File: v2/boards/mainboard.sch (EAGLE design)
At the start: 190 parts, among them IC1 LM2596S-ADJ, IC10 DRV8835, IC11 TSOP324, IC12 ESP-WROOM-32, IC13 PAM8403, IC15 MC1525, IC16 INA282, IC17 INA282, IC18 INA282, IC19 INA282, IC2 LM2596S-5.0, IC20 MCP3008, IC3 LD1117A, IC4 LM393, IC5 MCP101-300, IC6 TEENSY 3.6, IC7 PCA9634, IC8 PCA9554, IC9 PCA9634, J1 Bat_In, J10 SPI_0, J11 SPI_2, J12 SPI_2, J13 I2C_0, J14 I2C_1, J15 I2C_3, J16 BNO055, J17 Uart_2, J18 Uart_5, J19 Uart_6 (LP), J2 Erw_Pwr, J20 BPS, J21 Servo_2, J22 Servo_3, J23 Erw_Servo, J24 Erw_PWM, J25 ESP32_Uart, J26 SPEAKER_L, J27 SPEAKER_R, J28 AUDIO_TEENSY, J29 SWD, J3 I2C0_5V, J30 SWD_KL02, J31 Erw_ENA, J32 Erw_GPIO, J33 Erw_analog, J34 USB_Host, J35 ESP32_PROG, J4 I2C3_5V, J5 Servo_1, J6 H-Bridge Mode, J7 RC5_SEL, J8 SPI_0, J9 SPI_0, SW1 TL32PO, U1 IRL3103, U4 BS108, U5 BS108, U6 BS108, U7 BS108, U8 BS108, U9 BS108, X1 max. 18V

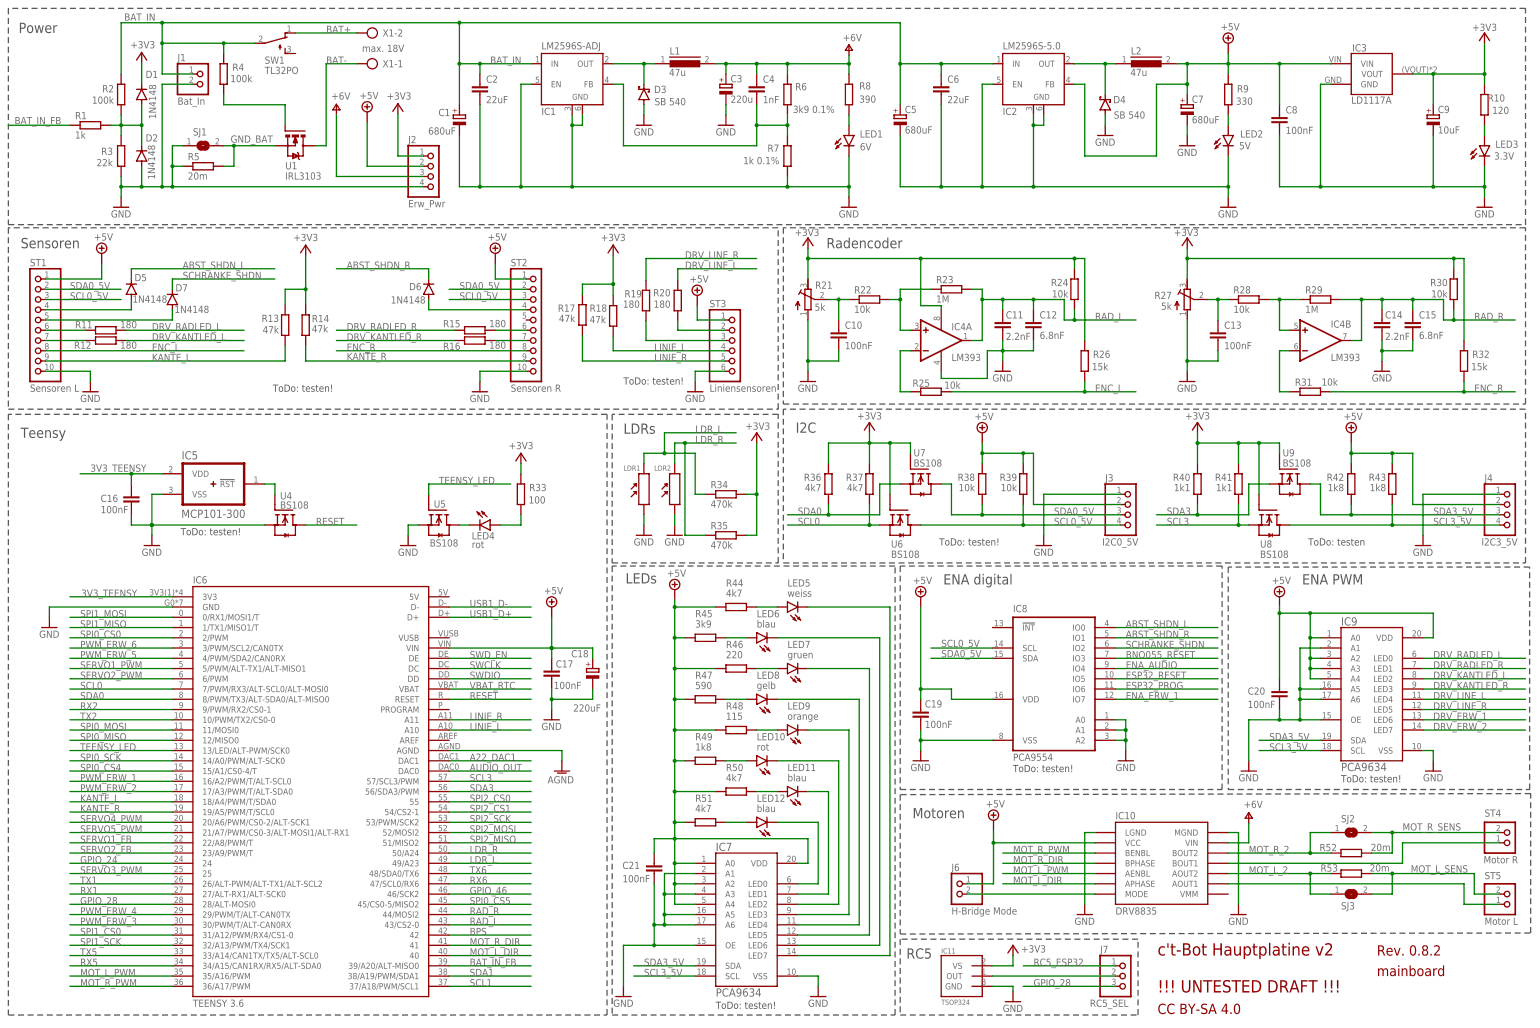
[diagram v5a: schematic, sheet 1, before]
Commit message: mainboard updated:
- some bugfixes after further testing
- discrete MCU board added
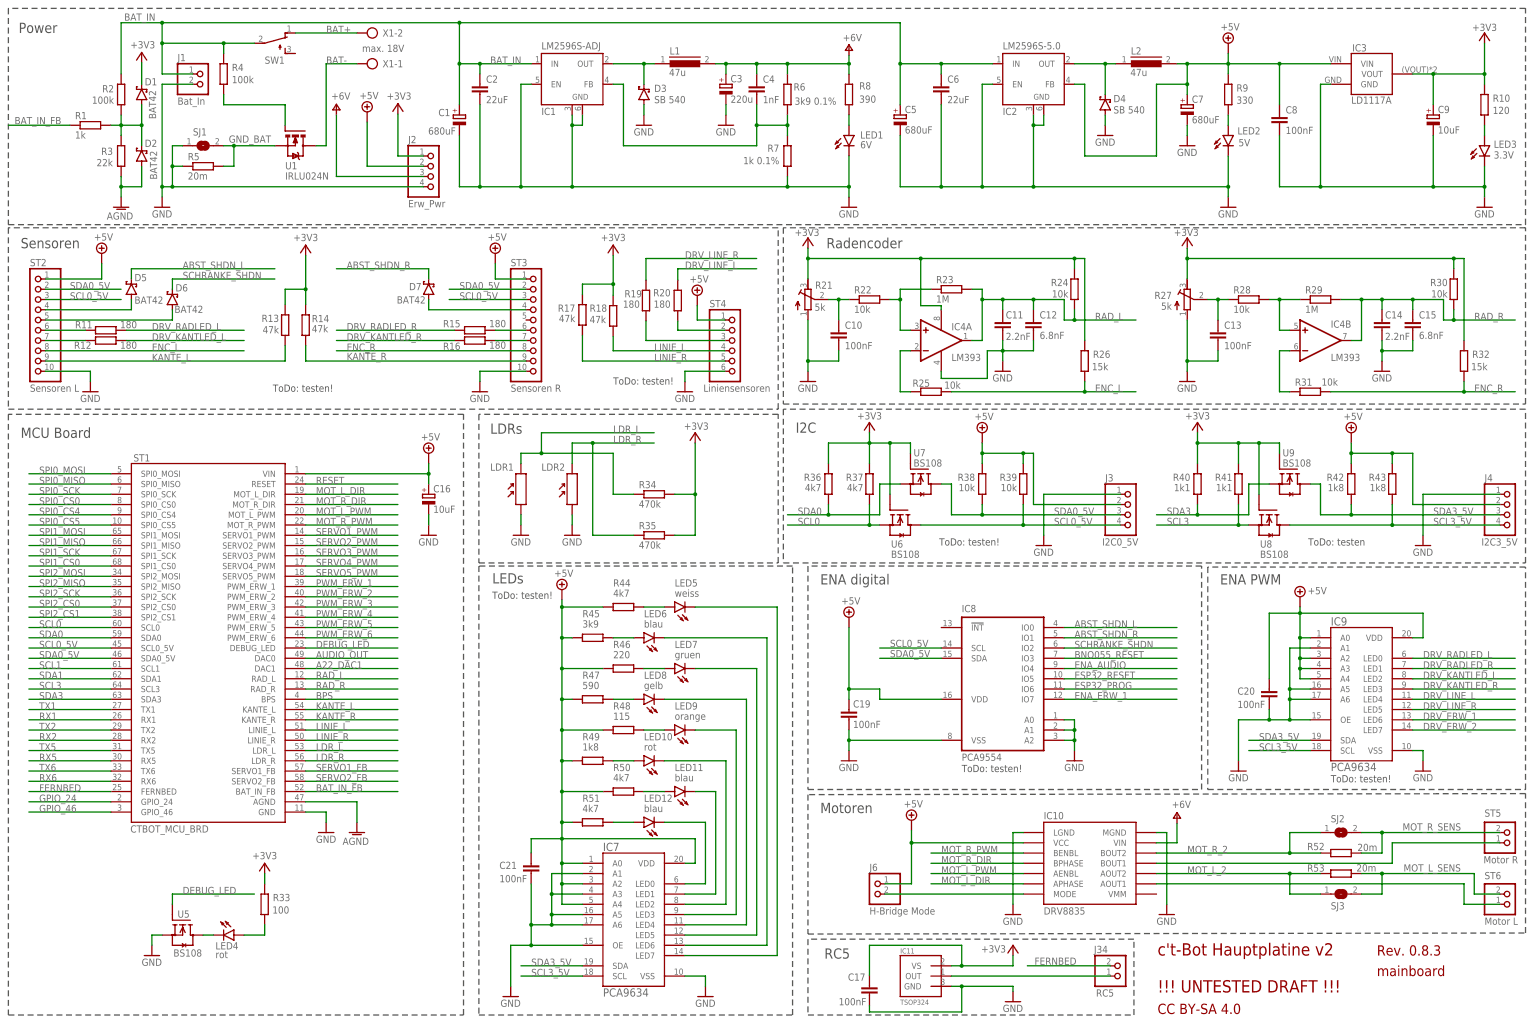
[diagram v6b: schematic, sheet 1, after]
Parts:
- removed BT1: CR2032, ct-bot:BATTERY-20MM_PTH
- removed IC5: MCP101-300, ct-bot:MCP101
- removed IC6: TEENSY 3.6, ct-bot:TEENSY3_6
- removed U4: BS108, ct-bot:BS108
- added J36: SPI1, ct-bot:PINHD-1X5
- added ST7: RPI_Interface, con-harting-ml:ML20
- C16: value 100nF -> 10uF; device rcl:C-EU025-025X050 -> rcl:CPOL-EUTT2D5L
- C18: value 220uF -> 100nF; device rcl:CPOL-EUE2-5 -> rcl:C-EU025-025X050
- D1, D2: value 1N4148 -> BAT42; device ct-bot:1N41480207/2V -> ct-bot:BAT42DO35-7
- D5, D6, D7, D8, D9: value 1N4148 -> BAT42; device ct-bot:1N41480207/2V -> ct-bot:BAT42"
- J29: device ct-bot:PINHD-1X6 -> ct-bot:PINHD-1X5
- J30: device ct-bot:PINHD90-1X2/90 -> ct-bot:PINHD-1X2
- J34: value USB_Host -> RC5; device ct-bot:PINHD-1X4 -> ct-bot:PINHD-1X2
- J7: value RC5_SEL -> ESP32_GPIO; SPICEPREFIX (none) -> J
- R1, R3, R55, R56, R57: device rcl:R-EU_0204/2V -> rcl:R-EU_0204/7
- R31, R32, R62: device rcl:R-EU_0204/7 -> rcl:R-EU_0204/2V
- ST1: value Sensoren L -> CTBOT_MCU_BRD; device ct-bot:PS25-10PS25-10 -> ct-bot:CTBOT_MCU_BRD
- ST2: value Sensoren R -> Sensoren L
- ST3: value Liniensensoren -> Sensoren R; device ct-bot:PS25-6 -> ct-bot:PS25-10PS25-10
- ST4: value Motor R -> Liniensensoren; device ct-bot:PINHD90-1X2/90 -> ct-bot:PS25-6
- ST5: value Motor L -> Motor R
- ST6: value RPI_Interface -> Motor L; device con-harting-ml:ML26 -> ct-bot:PINHD90-1X2/90
- U1: value IRL3103 -> IRLU024N; device ct-bot:IRF740 -> ct-bot:IRLU024NTO-251AA
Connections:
- removed net +5V: C17.1, C18.+, C19.1, C20.1, C21.1, C24.1, C25.1, C28.1, C29.+, C7.+, C8.1, IC10.VCC, IC13.PVDD, IC13.PVDD1, IC13.VDD, IC2.FB, IC3.VIN, IC6.VIN, IC7.A0, IC7.A2, IC7.A4, IC7.VDD, IC8.VDD, IC9.A0, IC9.A2, IC9.A3, IC9.A4, IC9.VDD, J10.1, J11.2, J12.2, J13.2, J14.2, J15.2, J16.1, J17.2, J18.2, J19.2, J2.2, J3.2, J34.1, J4.2, J6.1, J8.1, J9.1, L2.2, R38.2, R39.2, R42.2, R43.2, R44.1, R45.1, R46.1, R47.1, R48.1, R49.1, R50.1, R51.1, R9.2, ST1.1, ST2.1, ST3.1, ST6.23, ST6.25
- removed net 3V3_TEENSY: C16.1, IC5.VDD, IC6.3V3, J29.1
- removed net GPIO_28: IC6.28/ALT-MOSI0, J7.3
- removed net N$39: IC5.!RST, U4.G
- removed net RC5_ESP32: IC12.IO23, J7.1
- removed net SERVO3_FB: ST6.14
- removed net TEENSY_LED: IC6.13/LED/ALT-PWM/SCK0, U5.G
- removed net USB1_D+: IC6.D+, J34.3
- removed net USB1_D-: IC6.D-, J34.2
- removed net VBAT_RTC: BT1.+, IC6.VBAT
- new net DEBUG_LED: ST1.DEBUG_LED, U5.G
- new net RC5: IC11.OUT, J34.1
- new net VCC: C16.+, C19.1, C20.1, C21.1, C24.1, C25.1, C28.1, C29.+, C7.+, C8.1, IC10.VCC, IC13.PVDD, IC13.PVDD1, IC13.VDD, IC2.FB, IC3.VIN, IC7.A0, IC7.A2, IC7.A4, IC7.VDD, IC8.VDD, IC9.A0, IC9.A2, IC9.A3, IC9.A4, IC9.VDD, J10.1, J11.2, J12.2, J13.2, J14.2, J15.2, J16.1, J17.2, J18.2, J19.2, J2.2, J3.2, J4.2, J6.1, J8.1, J9.1, L2.2, R38.2, R39.2, R42.2, R43.2, R44.1, R45.1, R46.1, R47.1, R48.1, R49.1, R50.1, R51.1, R9.2, ST1.VIN, ST2.1, ST3.1, ST4.1, ST7.5
- net +3V3: now also C17.1, C18.1, ST7.3; no longer ST6.1
- net A22_DAC1: now also ST1.DAC1; no longer IC6.DAC1
- net ABST_SHDN_R: now also D7.C; no longer D6.C
- net AGND: now also D2.A, R3.1, ST1.AGND; no longer IC6.AGND
- net AUDIO_OUT: now also ST1.DAC0; no longer IC6.DAC0
- net BAT_IN_FB: now also ST1.BAT_IN_FB; no longer IC6.39/A20/ALT-MISO0
- net BPS: now also ST1.BPS; no longer IC6.42
- net ENC_L: now also ST2.8; no longer ST1.8
- net ENC_R: now also ST3.8; no longer ST2.8
- net FERNBED: now also J34.2, ST1.FERNBED; no longer IC11.OUT, J7.2
- net GND: now also C16.-, C18.2, J29.2, ST1.GND, ST3.10, ST4.6, ST7.20; no longer BT1.-, C16.2, C18.-, D2.A, IC5.VSS, IC6.GND, J29.3, J34.4, R3.1, ST1.10, ST3.6, ST6.24, ST6.26, U4.S
- net GPIO_24: now also ST1.GPIO_24; no longer IC6.24
- net GPIO_46: now also ST1.GPIO_46; no longer IC6.46/SCK2
- net IO34: now also J7.2
- net IO35: now also J7.1
- net IO36: now also J7.3
- net KANTE_L: now also ST1.KANTE_L, ST2.9; no longer IC6.18/A4/PWM/T/SDA0, ST1.9
- net KANTE_R: now also ST1.KANTE_R, ST3.9; no longer IC6.19/A5/PWM/T/SCL0, ST2.9
- net LDR_L: now also ST1.LDR_L; no longer IC6.49/A23
- net LDR_R: now also ST1.LDR_R; no longer IC6.50/A24
- net LINIE_L: now also ST1.LINIE_L, ST4.4; no longer IC6.A10, ST3.4
- net LINIE_R: now also ST1.LINIE_R, ST4.5; no longer IC6.A11, ST3.5
- net MOT_L_1: now also ST6.1; no longer ST5.1
- net MOT_L_DIR: now also ST1.MOT_L_DIR; no longer IC6.40
- net MOT_L_PWM: now also ST1.MOT_L_PWM; no longer IC6.35/A16/PWM
- net MOT_L_SENS: now also ST6.2; no longer ST5.2
- net MOT_R_1: now also ST5.1; no longer ST4.1
- net MOT_R_DIR: now also ST1.MOT_R_DIR; no longer IC6.41
- net MOT_R_PWM: now also ST1.MOT_R_PWM; no longer IC6.36/A17/PWM
- net MOT_R_SENS: now also ST5.2; no longer ST4.2
- net N$1: now also ST4.3; no longer ST3.3
- net N$30: now also ST4.2; no longer ST3.2
- net N$45: now also ST3.6; no longer ST2.6
- net N$47: now also ST2.6; no longer ST1.6
- net N$51: now also ST2.7; no longer ST1.7
- net N$53: now also ST3.7; no longer ST2.7
- net PWM_ERW_1: now also ST1.PWM_ERW_1; no longer IC6.16/A2/PWM/T/ALT-SCL0
- net PWM_ERW_2: now also ST1.PWM_ERW_2; no longer IC6.17/A3/PWM/T/ALT-SDA0
- net PWM_ERW_3: now also ST1.PWM_ERW_3; no longer IC6.30/PWM/T/ALT-CAN0RX
- net PWM_ERW_4: now also ST1.PWM_ERW_4; no longer IC6.29/PWM/T/ALT-CAN0TX
- net PWM_ERW_5: now also ST1.PWM_ERW_5; no longer IC6.4/PWM/SDA2/CAN0RX
- net PWM_ERW_6: now also ST1.PWM_ERW_6; no longer IC6.3/PWM/SCL2/CAN0TX
- net RAD_L: now also ST1.RAD_L; no longer IC6.43/CS2-0
- net RAD_R: now also ST1.RAD_R; no longer IC6.44/MOSI2
- net RESET: now also J29.1, ST1.RESET, ST7.13; no longer IC6.RESET, J29.2, ST6.12, U4.D
- net RPI_3V3: now also ST7.11; no longer ST6.11
- net RPI_SPI0_CE1: now also J36.5, ST7.15; no longer ST6.10
- net RX1: now also ST1.RX1, ST7.19; no longer IC6.27/ALT-RX1/ALT-SCK0, ST6.15
- net RX2: now also ST1.RX2; no longer IC6.9/PWM/RX2/CS0-1
- net RX5: now also ST1.RX5; no longer IC6.34/A15/CAN1RX/RX5/ALT-SDA0
- net RX6: now also ST1.RX6; no longer IC6.47/SCL0/RX6
- net SCHRANKE_SHDN: now also D6.C; no longer D7.C
- net SCL0: now also ST1.SCL0, ST7.12; no longer IC6.7/PWM/RX3/ALT-SCL0/ALT-MOSI0, ST6.21
- net SCL0_5V: now also ST1.SCL0_5V, ST3.3, ST7.7; no longer ST1.3, ST6.9
- net SCL1: now also ST1.SCL1; no longer IC6.37/A18/PWM/SCL1
- net SCL3: now also ST1.SCL3; no longer IC6.57/SCL3/PWM
- net SDA0: now also ST1.SDA0, ST7.10; no longer IC6.8/PWM/TX3/ALT-SDA0/ALT-MISO0, ST6.19
- net SDA0_5V: now also ST1.SDA0_5V, ST3.2, ST7.9; no longer ST1.2, ST6.7
- net SDA1: now also ST1.SDA1; no longer IC6.38/A19/PWM/SDA1
- net SDA3: now also ST1.SDA3; no longer IC6.56/SDA3/PWM
- net SERVO1_FB: now also ST1.SERVO1_FB; no longer IC6.22/A8/PWM/T
- net SERVO1_PWM: now also ST1.SERVO1_PWM; no longer IC6.5/PWM/ALT-TX1/ALT-MISO1
- net SERVO2_FB: now also ST1.SERVO2_FB, ST7.18; no longer IC6.23/A9/PWM/T, ST6.20
- net SERVO2_PWM: now also ST1.SERVO2_PWM, ST7.16; no longer IC6.6/PWM, ST6.18
- net SERVO3_PWM: now also ST1.SERVO3_PWM, ST7.14; no longer IC6.25, ST6.16
- net SERVO4_PWM: now also J10.6, ST1.SERVO4_PWM; no longer IC6.20/A6/PWM/CS0-2/ALT-SCK1
- net SERVO5_PWM: now also ST1.SERVO5_PWM; no longer IC6.21/A7/PWM/CS0-3/ALT-MOSI1/ALT-RX1, J10.6
- net SERVO_PWR: now also ST7.1; no longer ST6.22
- net SPI0_CS0: now also ST1.SPI0_CS0; no longer IC6.2/PWM
- net SPI0_CS4: now also ST1.SPI0_CS4; no longer IC6.15/A1/CS0-4/T
- net SPI0_CS5: now also ST1.SPI0_CS5; no longer IC6.45/CS0-5/MISO2
- net SPI0_MISO: now also ST1.SPI0_MISO; no longer IC6.12/MISO0
- net SPI0_MOSI: now also ST1.SPI0_MOSI; no longer IC6.11/MOSI0
- net SPI0_SCK: now also ST1.SPI0_SCK; no longer IC6.14/A0/PWM/ALT-SCK0
- net SPI1_CS0: now also J36.4, ST1.SPI1_CS0, ST7.2; no longer IC6.31/A12/PWM/RX4/CS1-0, ST6.8
- net SPI1_MISO: now also J36.2, ST1.SPI1_MISO, ST7.6; no longer IC6.1/TX1/MISO1/T, ST6.2
- net SPI1_MOSI: now also J36.1, ST1.SPI1_MOSI, ST7.8; no longer IC6.0/RX1/MOSI1/T, ST6.4
- net SPI1_SCK: now also J36.3, ST1.SPI1_SCK, ST7.4; no longer IC6.32/A13/PWM/TX4/SCK1, ST6.6
- net SPI2_CS0: now also ST1.SPI2_CS0; no longer IC6.55
- net SPI2_CS1: now also ST1.SPI2_CS1; no longer IC6.54/CS2-1
- net SPI2_MISO: now also ST1.SPI2_MISO; no longer IC6.51/MISO2
- net SPI2_MOSI: now also ST1.SPI2_MOSI; no longer IC6.52/MOSI2
- net SPI2_SCK: now also ST1.SPI2_SCK; no longer IC6.53/PWM/SCK2
- net SWCLK: now also J29.4; no longer IC6.DC, J29.5
- net SWDIO: now also J29.5; no longer IC6.DD, J29.6
- net SWD_EN: now also J29.3; no longer IC6.DE, J29.4
- net TX1: now also ST1.TX1, ST7.17; no longer IC6.26/ALT-PWM/ALT-TX1/ALT-SCL2, ST6.17
- net TX2: now also ST1.TX2; no longer IC6.10/PWM/TX2/CS0-0
- net TX5: now also ST1.TX5; no longer IC6.33/A14/CAN1TX/TX5/ALT-SCL0
- net TX6: now also ST1.TX6; no longer IC6.48/SDA0/TX6
- net VL53L0X_SHUT_L: now also ST2.4; no longer ST1.4
- net VL53L0X_SHUT_R: now also D7.A, ST3.4; no longer D6.A, ST2.4
- net VL6180X_SHDN: now also D6.A, ST2.5; no longer D7.A, ST1.5
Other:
- note added: "MCU Board"
- note added: "Rev. 0.8.3"
- note added: "ToDo: Signalauswahl"
- note added: "USB2Bot"
- note removed: "RTC BATTERIE"
- note removed: "Rev. 0.8.2"
- note removed: "Teensy"
- note removed: "ToDo: Signalauswahl + I2C3?"
- note removed: "USB HOST"
- note removed: "USB2Bot / Wi-Fi"
- moved on the sheet: C17, C19, C20, C21, IC10, IC11, IC7, IC8, IC9, J20, J6, LDR1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

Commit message: schematics and board files for ct-Bot v2 prototype
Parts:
- removed C27: 470nF, rcl:C-EU025-025X050
- removed C28: 1uF, rcl:C-EU025-025X050
- removed C29: 470uF, rcl:CPOL-EUE3.5-8
- removed D8, D9: BAT42, ct-bot:BAT42"
- removed IC11: TSOP324, ct-bot:TSOP324
- removed IC12: ESP-WROOM-32, ct-bot:ESP-WROOM-32
- removed IC13: PAM8403, ct-bot:PAM8403
- removed IC15: MC1525, ct-bot:MC1525TO
- removed IC16, IC17, IC18, IC19: INA282, ct-bot:INA28AID
- removed IC20: MCP3008, ct-bot:MCP3008SL
- removed J23: Erw_Servo, ct-bot:PINHD-1X2
- removed J24: Erw_PWM, ct-bot:PINHD-1X6
- removed J25: ESP32_Uart, ct-bot:PINHD-1X3
- removed J26: SPEAKER_L, ct-bot:PINHD-1X2
- removed J27: SPEAKER_R, ct-bot:PINHD-1X2
- removed J28: AUDIO_TEENSY, ct-bot:PINHD-1X3
- removed J29: SWD, ct-bot:PINHD-1X5
- removed J30: SWD_KL02, ct-bot:PINHD-1X2
- removed J31: Erw_ENA, ct-bot:PINHD-1X3
- removed J32: Erw_GPIO, ct-bot:PINHD-1X2
- removed J33: Erw_analog, ct-bot:PINHD-1X3
- removed J34: RC5, ct-bot:PINHD-1X2
- removed J35: ESP32_PROG, ct-bot:PINHD-1X3
- removed J36: SPI1, ct-bot:PINHD-1X5
- removed LDR1, LDR2: (no value), ct-bot:MPY54C569
- removed R45: 3k9, rcl:R-EU_0204/2V
- removed R46: 220, rcl:R-EU_0204/2V
- removed R47: 590, rcl:R-EU_0204/2V
- removed R48: 115, rcl:R-EU_0204/2V
- removed R49: 1k8, rcl:R-EU_0204/2V
- removed R50, R51: 4k7, rcl:R-EU_0204/2V
- removed R52, R53, R54: 20m, rcl:R-EU_R1210
- removed R55, R56, R57: 4k7, rcl:R-EU_0204/7
- removed R58, R59, R61, R62: 10k, rcl:R-EU_0204/2V
- removed R60: 5k, ct-bot:R-TRIMM64W
- removed SJ3, SJ4: (no value), jumper:SJ
- removed ST1: CTBOT_MCU_BRD, ct-bot:CTBOT_MCU_BRD
- removed ST2: Sensoren L, ct-bot:PS25-10PS25-10
- removed ST3: Sensoren R, ct-bot:PS25-10PS25-10
- removed ST4: Liniensensoren, ct-bot:PS25-6
- removed ST5: Motor R, ct-bot:PINHD90-1X2/90
- removed ST6: Motor L, ct-bot:PINHD90-1X2/90
- removed ST7: RPI_Interface, con-harting-ml:ML20
- removed U5, U6, U7, U8, U9: BS108, ct-bot:BS108
- added IC5: (no value), ct-bot:INA28AID
- added IC6: PCA9634, ct-bot:PCA9634-SO20
- added L3: 3u3, ct-bot:07HCP-3U3
- added MCU: CTBOT_MCU_BRD_V2, ct-bot:CTBOT_MCU_BRD_V2
- added S1, S2: Reset, SparkFun-Switches:MOMENTARY-SWITCH-SPST-PTH-6.0MM
- added U$10: IMU, ct-bot:NXP_9DOF
- added U2, U3, U4: BS108, ct-bot:BS108
- added X2: Sensoren L, ct-bot:08-JST
- added X3: Sensoren R, ct-bot:08-JST
- added X4: Liniensensoren, ct-bot:06-JST-B6B-XH-A
- added X5: Motorctrl, ct-bot:08-JST
- C10: value 100nF -> 10uF; device rcl:C-EU025-025X050 -> rcl:CPOL-EUE2-5
- C11: value 2.2nF -> 1nF
- C12: value 6.8nF -> 100nF; device rcl:C-EU025-025X050 -> rcl:C-EUC0805
- C13: device rcl:C-EU025-025X050 -> rcl:C-EUC0805
- C14: value 2.2nF -> 10uF; device rcl:C-EU025-025X050 -> rcl:CPOL-EUTT2D5L
- C15: value 6.8nF -> 1nF
- C16: value 10uF -> 100nF; device rcl:CPOL-EUTT2D5L -> rcl:C-EU025-025X050
- C21: value 100nF -> 470nF
- C22: value 10uF -> 470nF; device rcl:CPOL-EUE2.5-5 -> rcl:C-EU025-025X050
- C23: value 470nF -> 1uF
- C24: value 1uF -> 100nF
- C26: value 100nF -> 470uF; device rcl:C-EU025-025X050 -> rcl:CPOL-EUE3.5-8
- C3: value 220u -> 220uF
- C7: value 680uF -> 220uF
- C8: value 100nF -> 180uF; device rcl:C-EU025-025X050 -> rcl:CPOL-EUE3.5-8
- C9: value 10uF -> 100nF; device rcl:CPOL-EUE2-5 -> rcl:C-EU025-025X050
- IC10: value DRV8835 -> PAM8403; device ct-bot:DRV8835THROUGHHOLE -> ct-bot:PAM8403
- IC4: value LM393 -> (none); device linear:LM393N -> ct-bot:INA28AID; SPICEPREFIX J -> (none)
- IC7: value PCA9634 -> PCA9554; device ct-bot:PCA9634-SO20 -> ct-bot:PCA9554D
- IC8: value PCA9554 -> PCA9634; device ct-bot:PCA9554D -> ct-bot:PCA9634-SO20
- IC9: value PCA9634 -> TSOP324; device ct-bot:PCA9634-SO20 -> ct-bot:TSOP324
- J10: value SPI_0 -> I2C_2; device ct-bot:PINHD-1X6 -> ct-bot:PINHD-1X4
- J11: value SPI_2 -> I2C_3; device ct-bot:PINHD-1X7 -> ct-bot:PINHD-1X4
- J12: value SPI_2 -> Uart_1; device ct-bot:PINHD-1X6 -> ct-bot:PINHD-1X4
- J13: value I2C_0 -> Servo_2
- J14: value I2C_1 -> Servo_3
- J15: value I2C_3 -> Servo_4; device ct-bot:PINHD-1X4 -> ct-bot:PINHD-1X3
- J16: value BNO055 -> RPi_Interface; device ct-bot:PINHD-1X6 -> con-harting-ml:ML10
- J17: value Uart_2 -> Audio; device ct-bot:PINHD-1X4 -> ct-bot:PINHD-1X3
- J18: value Uart_5 -> Erw_DRV
- J19: value Uart_6 (LP) -> Erw_ENA
- J20: value BPS -> SPEAKER_R; device ct-bot:PINHD-1X3 -> ct-bot:PINHD-1X2
- J21: value Servo_2 -> SPEAKER_L; device ct-bot:PINHD-1X4 -> ct-bot:PINHD-1X2
- J22: value Servo_3 -> AUDIO_IN; device ct-bot:PINHD-1X4 -> ct-bot:PINHD-1X3
- J3: value I2C0_5V -> I2C1_5V
- J4: value I2C3_5V -> I2C_1
- J5: value Servo_1 -> BPS; device ct-bot:PINHD-1X4 -> ct-bot:PINHD-1X3
- J6: value H-Bridge Mode -> Servo_1; device ct-bot:PINHD-1X2 -> ct-bot:PINHD-1X4
- J7: value ESP32_GPIO -> SPI_1; device ct-bot:PINHD-1X3 -> con-harting-ml:ML10; SPICEPREFIX J -> (none)
- J8: value SPI_0 -> SPI_1; device con-harting-ml:ML10 -> ct-bot:PINHD-1X7
- J9: value SPI_0 -> SPI_1; device ct-bot:PINHD-1X7 -> ct-bot:PINHD-1X6
- R10: value 120 -> 180
- R11, R12: value 180 -> 47k
- R13, R17: value 47k -> 180
- R14, R2, R37: device rcl:R-EU_0204/2V -> rcl:R-EU_0204/7
- R15: value 180 -> 47k; device rcl:R-EU_0204/2V -> rcl:R-EU_0204/7
- R18: value 47k -> 330
- R19: value 180 -> 30m; device rcl:R-EU_0204/2V -> rcl:R-EU_R2512
- R20: value 180 -> 100m; device rcl:R-EU_0204/2V -> rcl:R-EU_R2512
- R21: value 5k -> 4k7; device ct-bot:R-TRIMM64W -> rcl:R-EU_0204/7
- R22, R38, R39: value 10k -> 4k7; device rcl:R-EU_0204/2V -> rcl:R-EU_0204/7
- R23: value 1M -> 10k
- R25: value 10k -> 1k1; device rcl:R-EU_0204/2V -> rcl:R-EU_0204/7
- R26: value 15k -> 1k1; device rcl:R-EU_0204/2V -> rcl:R-EU_0204/7
- R27: value 5k -> 1k8; device ct-bot:R-TRIMM64W -> rcl:R-EU_0204/2V
- R28: value 10k -> 330; device rcl:R-EU_0204/7 -> rcl:R-EU_0204/2V
- R29: value 1M -> 27k; device rcl:R-EU_0204/7 -> rcl:R-EU_0204/2V
- R30: device rcl:R-EU_0204/7 -> rcl:R-EU_0204/2V
- R31: value 10k -> 15k
- R32: value 15k -> 2k2
- R33: value 100 -> 2k2
- R34: value 470k -> 1k8
- R35: value 470k -> 10k
- R36, R44: value 4k7 -> 10k
- R40: value 1k1 -> 4k7; device rcl:R-EU_0204/2V -> rcl:R-EU_0204/7
- R41: value 1k1 -> 5k; device rcl:R-EU_0204/2V -> ct-bot:R-TRIMM64W
- R42: value 1k8 -> 5k; device rcl:R-EU_0204/2V -> ct-bot:R-TRIMM64W
- R43: value 1k8 -> 10k
- R5: value 20m -> 3k9 0.1%; device rcl:R-EU_R1210 -> rcl:R-EU_0204/2V
- R6: value 3k9 0.1% -> 1k 0.1%
- R7: value 1k 0.1% -> 27k
- R8: value 390 -> 22k
- R9: value 330 -> 15k
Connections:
- net V5_L1 renamed V5_L2
- removed net A22_DAC1: J33.1, ST1.DAC1
- removed net AUDIO_OUT: J28.1, J33.2, ST1.DAC0
- removed net BAT_CUR: IC17.OUT, IC20.CH0
- removed net BNO055_RESET: IC8.IO3, J16.6
- removed net DRV_RADLED_L: IC9.LED0, R11.2
- removed net DRV_RADLED_R: IC9.LED1, R15.1
- removed net EN: D8.A, IC12.EN, R59.1
- removed net ENC_L: R25.2, R26.1, ST2.8
- removed net ENC_R: R31.2, R32.1, ST3.8
- removed net ESP32_PROG: D9.C, IC8.IO6, J35.2
- removed net ESP32_RESET: D8.C, IC8.IO5, J35.3
- removed net GND_BAT: IC17.-IN, R5.2, SJ1.2, U1.S
- removed net GPIO_24: J32.1, ST1.GPIO_24
- removed net GPIO_46: J32.2, ST1.GPIO_46
- removed net IO0: D9.A, IC12.IO0, R58.2
- removed net IO10: IC12.SD3
- removed net IO11: IC12.CMD
- removed net IO13: IC12.IO13
- removed net IO15: IC12.IO15
- removed net IO18: IC12.IO18
- removed net IO19: IC12.IO19
- removed net IO21: IC12.IO21
- removed net IO34: IC12.IO34, J7.2
- removed net IO35: IC12.IO35, J7.1
- removed net IO36: IC12.SENSOR_VP, J7.3
- removed net IO39: IC12.SENSOR_VN
- removed net IO4: IC12.IO4
- removed net IO5: IC12.IO5
- removed net IO6: IC12.CLK
- removed net IO7: IC12.SDO
- removed net IO8: IC12.SD1
- removed net IO9: IC12.SD2
- removed net KL02_DC: IC12.IO12, J30.1
- removed net KL02_DD: IC12.IO14, J30.2
- removed net LDR_L: LDR1.P$2, R34.1, ST1.LDR_L
- removed net LDR_R: LDR2.P$2, R35.1, ST1.LDR_R
- removed net MCP_CH4: IC20.CH4
- removed net MCP_CH5: IC20.CH5
- removed net MCP_CH6: IC20.CH6
- removed net MCP_CH7: IC20.CH7
- removed net MOT_L_1: IC10.AOUT1, ST6.1
- removed net MOT_L_2: IC10.AOUT2, IC18.+IN, R53.1, SJ3.1
- removed net MOT_L_CUR: IC18.OUT, IC20.CH1
- removed net MOT_L_DIR: IC10.APHASE, ST1.MOT_L_DIR
- removed net MOT_L_PWM: IC10.AENBL, ST1.MOT_L_PWM
- removed net MOT_L_SENS: IC18.-IN, R53.2, SJ3.2, ST6.2
- removed net MOT_R_1: IC10.BOUT1, ST5.1
- removed net MOT_R_2: IC10.BOUT2, IC19.+IN, R52.1, SJ2.1
- removed net MOT_R_CUR: IC19.OUT, IC20.CH2
- removed net MOT_R_DIR: IC10.BPHASE, ST1.MOT_R_DIR
- removed net MOT_R_PWM: IC10.BENBL, ST1.MOT_R_PWM
- removed net MOT_R_SENS: IC19.-IN, R52.2, SJ2.2, ST5.2
- removed net N$10: IC4B.-IN, R31.1
- removed net N$3: IC10.MODE, J6.2
- removed net N$34: C10.1, R21.S, R22.1
- removed net N$35: IC4A.+IN, R22.2, R23.1
- removed net N$36: C13.1, R27.S, R28.1
- removed net N$37: IC4B.+IN, R28.2, R29.1
- removed net N$45: R15.2, ST3.6
- removed net N$47: R11.1, ST2.6
- removed net PWM_ERW_1: J24.1, ST1.PWM_ERW_1
- removed net PWM_ERW_2: J24.2, ST1.PWM_ERW_2
- removed net PWM_ERW_3: J24.3, J8.9, ST1.PWM_ERW_3
- removed net PWM_ERW_4: J24.4, ST1.PWM_ERW_4
- removed net PWM_ERW_5: J24.5, ST1.PWM_ERW_5
- removed net PWM_ERW_6: J24.6, ST1.PWM_ERW_6
- removed net RAD_L: C11.1, C12.1, IC4A.OUT, R23.2, R24.1, ST1.RAD_L
- removed net RAD_R: C14.1, C15.1, IC4B.OUT, R29.2, R30.1, ST1.RAD_R
- removed net RC5: IC11.OUT, J34.1
- removed net REF_2.5: IC15.VO, IC18.REF2, IC19.REF2, IC20.VREF
- removed net RPI_3V3: ST7.11
- removed net RPI_SPI0_CE1: J36.5, ST7.15
- removed net RX5: IC12.IO17, J18.4, ST1.RX5
- removed net RX6: J19.4, ST1.RX6
- removed net RXD0: IC12.RXD0, J25.3
- removed net SCL0: J13.4, R37.1, ST1.SCL0, ST7.12, U6.S
- removed net SCL0_5V: IC8.SCL, J16.5, J3.4, R39.1, ST1.SCL0_5V, ST2.3, ST3.3, ST7.7, U6.D
- removed net SCL3_5V: IC7.SCL, IC9.SCL, J4.4, R43.1, U8.D
- removed net SDA0: J13.3, R36.1, ST1.SDA0, ST7.10, U7.S
- removed net SDA0_5V: IC8.SDA, J16.4, J3.3, R38.1, ST1.SDA0_5V, ST2.2, ST3.2, ST7.9, U7.D
- removed net SDA3_5V: IC7.SDA, IC9.SDA, J4.3, R42.1, U9.D
- removed net SERVO5_PWM: IC20.!CS, J23.2, J9.7, ST1.SERVO5_PWM
- removed net SERVO_CUR: IC16.OUT, IC20.CH3
- removed net SERVO_PWR: IC16.-IN, J21.2, J22.2, J5.2, R54.2, SJ4.2, ST7.1
- removed net SPI0_CS0: J8.6, ST1.SPI0_CS0
- removed net SPI0_CS4: J8.7, ST1.SPI0_CS4
- removed net SPI0_CS5: J8.8, ST1.SPI0_CS5
- removed net SPI0_MISO: IC20.MISO, J10.4, J8.4, J9.4, ST1.SPI0_MISO
- removed net SPI0_MOSI: IC20.MOSI, J10.3, J8.3, J9.3, ST1.SPI0_MOSI
- removed net SPI0_SCK: IC20.SCK, J10.5, J8.5, J9.5, ST1.SPI0_SCK
- removed net SPI1_CS0: J36.4, ST1.SPI1_CS0, ST7.2
- removed net SPI2_CS0: J11.6, ST1.SPI2_CS0
- removed net SWCLK: IC12.IO33, J29.4
- removed net SWDIO: IC12.IO32, J29.5
- removed net SWD_EN: IC12.IO27, J29.3
- removed net TX5: IC12.IO16, J18.3, ST1.TX5
- removed net TX6: J19.3, ST1.TX6
- removed net TXD0: IC12.TXD0, J25.2
- removed net VCC: C16.+, C19.1, C20.1, C21.1, C24.1, C25.1, C28.1, C29.+, C7.+, C8.1, IC10.VCC, IC13.PVDD, IC13.PVDD1, IC13.VDD, IC2.FB, IC3.VIN, IC7.A0, IC7.A2, IC7.A4, IC7.VDD, IC8.VDD, IC9.A0, IC9.A2, IC9.A3, IC9.A4, IC9.VDD, J10.1, J11.2, J12.2, J13.2, J14.2, J15.2, J16.1, J17.2, J18.2, J19.2, J2.2, J3.2, J4.2, J6.1, J8.1, J9.1, L2.2, R38.2, R39.2, R42.2, R43.2, R44.1, R45.1, R46.1, R47.1, R48.1, R49.1, R50.1, R51.1, R9.2, ST1.VIN, ST2.1, ST3.1, ST4.1, ST7.5
- new net +5V: C14.+, C16.1, C17.1, C18.1, C23.1, C25.1, C26.+, C9.1, IC10.PVDD, IC10.PVDD1, IC10.VDD, IC3.VIN, IC4.-IN, IC6.A0, IC6.A2, IC6.A4, IC6.VDD, IC7.VDD, IC8.A0, IC8.A2, IC8.A3, IC8.A4, IC8.VDD, J10.2, J11.2, J12.2, J16.7, J2.2, J3.2, J4.2, J7.1, J8.1, J9.1, MCU.+5V, R19.2, R23.2, R24.2, R27.2, R29.1, R30.1, R31.1, R32.1, R33.1, R34.1, R35.1, R36.1, R8.2, SJ1.2, X2-1.1, X3-1.1, X4-1.1, X5-1.1
- new net 5V_SUPPLY: C8.+, IC4.+IN, L3.2, R19.1, SJ1.1
- new net 6V_SERVO: IC5.-IN, J13.2, J14.2, J15.2, J16.9, J6.2, R20.2, SJ2.2
- new net AUDIO_L: J17.2, MCU.AUDIO_L
- new net AUDIO_R: J17.3, MCU.AUDIO_R
- new net CURRENT_5V: IC4.OUT, MCU.CURRENT_5V
- new net CURRENT_SERVO: IC5.OUT, MCU.CURRENT_SERVO
- new net DRV_DISPLAY: IC8.LED6, J7.9
- new net DRV_ERW_3: IC8.LED7, J18.2
- new net ENA_ERW_2: IC7.IO5, J19.3
- new net GPIO1: J8.6, J9.6, MCU.GPIO1
- new net GPIO2: J8.7, MCU.GPIO2
- new net IMU_RST: IC7.IO7, J19.2, U$10.RST
- new net MCTRL_RESET: C11.1, IC7.IO6, R18.2, X5-7.1
- new net N$14: R28.1, S2.2
- new net N$39: C22.2, R42.S
- new net SCL1_5V: IC6.SCL, IC7.SCL, IC8.SCL, J3.4, R24.1, U2.D, X2-3.1, X3-3.1
- new net SCL2: J10.3, MCU.SCL2, R26.1, U$10.SCL
- new net SDA1_5V: IC6.SDA, IC7.SDA, IC8.SDA, J3.3, R23.1, U3.D, X2-2.1, X3-2.1
- new net SDA2: J10.4, MCU.SDA2, R25.1, U$10.SDA
- new net SERVO3_FB: J14.4, MCU.SERVO3_FB
- new net SPI1_CS1: J7.6, MCU.SPI1_CS1
- new net SPI1_CS2: J7.7, MCU.SPI1_CS2
- new net SPI1_CS3: J7.8, MCU.SPI1_CS3
- new net V5_L3: C7.+, IC2.FB, L2.2, L3.1
- net +3V3: now also C10.+, C12.1, C13.1, C19.1, C20.1, IC4.V+, IC5.V+, IC9.VS, J16.5, J5.3, J7.10, MCU.+3V3, R11.2, R12.1, R14.2, R15.2, R21.2, R22.2, R25.2, R38.2, R39.2, R9.2, U$10.VIN, U2.G, U3.G; no longer C17.1, C18.1, C22.+, C9.+, IC11.VS, IC12.3V3, IC15.VIN, IC16.V+, IC17.V+, IC18.V+, IC19.V+, IC20.VDD, IC4P.V+, J20.3, J8.10, R10.2, R13.2, R14.1, R17.2, R18.2, R21.E, R24.2, R27.E, R30.2, R32.2, R33.2, R34.2, R35.2, R36.2, R41.2, R55.2, R56.2, R57.2, R58.1, R59.2, ST7.3, U6.G, U7.G, U8.G, U9.G
- net +6V: now also IC5.+IN, R20.1, R5.2, R7.1, SJ2.1, X5-2.1; no longer IC10.VIN, IC16.+IN, J2.3, R54.1, R6.2, R8.1, SJ4.1
- net ABST_SHDN_L: now also IC7.IO0; no longer IC8.IO0
- net ABST_SHDN_R: now also IC7.IO2; no longer IC8.IO1
- net AGND: now also C23.2, C24.2, IC10.GND, J17.1, J22.1, MCU.AGND, R41.E, R42.E; no longer C25.2, C26.2, IC13.GND, IC15.GND, IC16.GND, IC16.REF1, IC16.REF2, IC17.GND, IC17.REF1, IC17.REF2, IC18.GND, IC18.REF1, IC19.GND, IC19.REF1, IC20.AGND, J33.3, R60.E, ST1.AGND
- net BAT_IN: now also J16.3
- net BAT_IN_FB: now also MCU.BAT_IN_FB; no longer ST1.BAT_IN_FB
- net BPS: now also J5.1, MCU.BPS; no longer J20.1, ST1.BPS
- net DEBUG_LED: now also MCU.DEBUG_LED, U4.G; no longer ST1.DEBUG_LED, U5.G
- net DRV_ERW_1: now also IC8.LED3, J18.4; no longer IC9.LED6, J31.2
- net DRV_ERW_2: now also IC8.LED2, J18.3; no longer IC9.LED7, J31.3
- net DRV_KANTLED_L: now also IC8.LED0, R10.2; no longer IC9.LED2, R12.2
- net DRV_KANTLED_R: now also IC8.LED1, R13.1; no longer IC9.LED3, R16.1
- net DRV_LINE_L: now also IC8.LED4, R17.2; no longer IC9.LED4, R20.2
- net DRV_LINE_R: now also IC8.LED5, R16.2; no longer IC9.LED5, R19.2
- net ENA_AUDIO: now also IC10.SHND, IC7.IO3; no longer IC13.SHND, IC8.IO4
- net ENA_ERW_1: now also IC7.IO4, J19.4; no longer IC8.IO7, J31.1
- net FERNBED: now also IC9.OUT, MCU.FERNBED; no longer J34.2, ST1.FERNBED
- net GND: now also C10.-, C14.-, C16.2, C25.2, C26.-, C8.-, C9.2, IC10.PGND, IC10.PGND1, IC4.GND, IC4.REF1, IC4.REF2, IC5.GND, IC5.REF1, IC5.REF2, IC6.A1, IC6.A3, IC6.A5, IC6.A6, IC6.OE, IC6.VSS, IC7.A0, IC7.A2, IC8.A5, IC8.A6, IC8.OE, IC9.GND, J10.1, J16.1, J16.2, J2.3, J5.2, J6.1, J7.2, MCU.GND, R6.1, S1.1, S2.1, U$10.GND, U1.S, U4.S, X2-8.1, X3-8.1, X4-6.1, X5-8.1; no longer C10.2, C14.2, C16.-, C21.2, C22.-, C24.2, C28.2, C29.-, C8.2, C9.-, IC10.LGND, IC10.MGND, IC11.GND, IC12.GND@1, IC12.GND@15, IC12.GND@38, IC12.IO2, IC13.PGND, IC13.PGND1, IC17.+IN, IC20.GND, IC4P.V-, IC7.A3, IC7.A5, IC7.A6, IC7.OE, IC8.A0, IC8.A2, IC9.A1, IC9.A5, IC9.A6, IC9.OE, IC9.VSS, J10.2, J16.3, J17.1, J20.2, J21.1, J22.1, J25.1, J29.2, J35.1, J5.1, LDR1.P$1, LDR2.P$1, R21.A, R27.A, R5.1, R7.1, SJ1.1, ST1.GND, ST2.10, ST3.10, ST4.6, ST7.20, U5.S
- net KANTE_L: now also MCU.KANTE_L, R11.1, X2-7.1; no longer R13.1, ST1.KANTE_L, ST2.9
- net KANTE_R: now also MCU.KANTE_R, R12.2, X3-7.1; no longer R14.2, ST1.KANTE_R, ST3.9
- net LINE_IN_L: now also J22.2, R41.A; no longer J28.2, R60.A
- net LINE_IN_R: now also J22.3, R42.A; no longer C27.2, J28.3
- net LINIE_L: now also MCU.LINIE_L, R15.1, X4-4.1; no longer R18.1, ST1.LINIE_L, ST4.4
- net LINIE_R: now also MCU.LINIE_R, R14.1, X4-5.1; no longer R17.1, ST1.LINIE_R, ST4.5
- net N$1: now also R16.1, X4-3.1; no longer R19.1, ST4.3
- net N$11: now also R8.1; no longer R9.1
- net N$13: now also IC6.LED2; no longer IC7.LED2
- net N$15: now also IC6.LED3; no longer IC7.LED3
- net N$16: now also IC6.LED4; no longer IC7.LED4
- net N$17: now also IC6.LED5; no longer IC7.LED5
- net N$18: now also IC6.LED6; no longer IC7.LED6
- net N$19: now also IC6.LED7; no longer IC7.LED7
- net N$2: now also R9.1; no longer R10.1
- net N$20: now also R29.2; no longer R44.2
- net N$21: now also R30.2; no longer R45.2
- net N$22: now also R31.2; no longer R46.2
- net N$23: now also R32.2; no longer R47.2
- net N$24: now also R33.2; no longer R48.2
- net N$25: now also R34.2; no longer R49.2
- net N$26: now also R35.2; no longer R50.2
- net N$27: now also R36.2; no longer R51.2
- net N$28: now also R27.1; no longer R33.1
- net N$29: now also U4.D; no longer U5.D
- net N$30: now also R17.1, X4-2.1; no longer R20.1, ST4.2
- net N$31: now also IC10.+OUT_L, J21.2; no longer IC13.+OUT_L, J26.2
- net N$32: now also IC10.-OUT_L, J21.1; no longer IC13.-OUT_L, J26.1
- net N$33: now also C24.1, IC10.VREF; no longer C26.1, IC13.VREF
- net N$40: now also IC10.INL, R43.1; no longer IC13.INL, R61.1
- net N$41: now also C21.1, R43.2; no longer C23.1, R61.2
- net N$42: now also C21.2, R41.S; no longer C23.2, R60.S
- net N$43: now also IC10.-OUT_R, J20.1; no longer IC13.-OUT_R, J27.1
- net N$44: now also IC10.+OUT_R, J20.2; no longer IC13.+OUT_R, J27.2
- net N$46: now also IC10.INR, R44.1; no longer IC13.INR, R62.1
- net N$48: now also C22.1, R44.2; no longer C27.1, R62.2
- net N$5: now also R18.1, S1.2; no longer IC4A.-IN, R25.1
- net N$51: now also R10.1, X2-6.1; no longer R12.1, ST2.7
- net N$53: now also R13.2, X3-6.1; no longer R16.2, ST3.7
- net N$6: now also IC6.LED0; no longer IC7.LED0
- net N$7: now also IC6.LED1; no longer IC7.LED1
- net N$8: now also R7.2; no longer R8.2
- net N$9: now also R5.1, R6.2; no longer R6.1, R7.2
- net RESET: now also C15.1, MCU.RESET, R28.2; no longer IC12.IO22, J29.1, ST1.RESET, ST7.13
- net RX1: now also J12.4, MCU.RX1, X5-5.1; no longer ST1.RX1, ST7.19
- net RX2: now also MCU.RX2, X5-3.1; no longer J17.4, ST1.RX2
- net SCHRANKE_SHDN: now also IC7.IO1; no longer IC8.IO2
- net SCL1: now also J4.4, MCU.SCL1, R22.1, U2.S; no longer J14.4, ST1.SCL1
- net SCL3: now also J11.3, MCU.SCL3; no longer IC12.IO26, J15.3, R41.1, ST1.SCL3, U8.S
- net SDA1: now also J4.3, MCU.SDA1, R21.1, U3.S; no longer J14.3, ST1.SDA1
- net SDA3: now also J11.4, MCU.SDA3; no longer IC12.IO25, J15.4, R40.1, ST1.SDA3, U9.S
- net SERVO1_FB: now also J6.4, MCU.SERVO1_FB; no longer J5.4, ST1.SERVO1_FB
- net SERVO1_PWM: now also J6.3, MCU.SERVO1_PWM, R37.1; no longer J5.3, R55.1, ST1.SERVO1_PWM
- net SERVO2_FB: now also J13.4, MCU.SERVO2_FB; no longer J21.4, ST1.SERVO2_FB, ST7.18
- net SERVO2_PWM: now also J13.3, MCU.SERVO2_PWM, R38.1; no longer J21.3, R56.1, ST1.SERVO2_PWM, ST7.16
- net SERVO3_PWM: now also J14.3, MCU.SERVO3_PWM, R39.1; no longer J22.3, R57.1, ST1.SERVO3_PWM, ST7.14
- net SERVO4_PWM: now also J15.3, MCU.SERVO4_PWM, R40.1; no longer J10.6, J23.1, J9.6, ST1.SERVO4_PWM
- net SPI1_MISO: now also J7.4, J8.4, J9.4, MCU.SPI1_MISO; no longer J36.2, ST1.SPI1_MISO, ST7.6
- net SPI1_MOSI: now also J7.3, J8.3, J9.3, MCU.SPI1_MOSI; no longer J36.1, ST1.SPI1_MOSI, ST7.8
- net SPI1_SCK: now also J7.5, J8.5, J9.5, MCU.SPI1_SCK; no longer J36.3, ST1.SPI1_SCK, ST7.4
- net SPI2_CS1: now also J16.4, MCU.SPI2_CS1; no longer J11.7, J12.6, ST1.SPI2_CS1
- net SPI2_MISO: now also J16.8, MCU.SPI2_MISO; no longer J11.4, J12.4, ST1.SPI2_MISO
- net SPI2_MOSI: now also J16.6, MCU.SPI2_MOSI; no longer J11.3, J12.3, ST1.SPI2_MOSI
- net SPI2_SCK: now also J16.10, MCU.SPI2_SCK; no longer J11.5, J12.5, ST1.SPI2_SCK
- net TX1: now also J12.3, MCU.TX1, X5-6.1; no longer ST1.TX1, ST7.17
- net TX2: now also MCU.TX2, X5-4.1; no longer J17.3, ST1.TX2
- net VL53L0X_SHUT_L: now also X2-4.1; no longer ST2.4
- net VL53L0X_SHUT_R: now also X3-4.1; no longer ST3.4
- net VL6180X_SHDN: now also X2-5.1; no longer ST2.5
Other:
- note added: "I2C 2"
- note added: "I2C 3"
- note added: "IMU"
- note added: "Rev. 0.9.2"
- note added: "SERVO"
- note added: "Timo Sandmann, CC BY-SA 4.0"
- note added: "UART 1"
- note added: "Widerstände an LEDs anpassen"
- note added: "ct-Bot v2 Mainboard"
- note added: "ct-Bot v2 Mainboard (optionale Parts)"
- note removed: "(optional)"
- note removed: "CC BY-SA 4.0"
- note removed: "LDRs"
- note removed: "Radencoder"
- note removed: "Rev. 0.8.3"
- note removed: "SERVO / PWM"
- note removed: "STROMMESSUNG"
- note removed: "SWD DEBUG PORT"
- note removed: "ToDo: Signalauswahl"
- note removed: "ToDo: testen"
- note removed: "ToDo: testen!"
- note removed: "UART"
- note removed: "USB2Bot"
- note removed: "WIFI-Modul"
- note removed: "c't-Bot Hauptplatine v2 !!! UNTESTED DRAFT !!!"
- note removed: "c't-Bot Hauptplatine v2 (optionale Parts) !!! UNTESTED DRAFT !!!"
- note removed: "mainboard"
- moved on the sheet: C1, C11, C12, C13, C15, C17, C19, C2, C20, C23, C24, C25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
